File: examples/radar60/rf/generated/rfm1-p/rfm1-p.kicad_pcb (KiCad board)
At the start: 6 copper layers, 40.1 x 23.8 mm, 18 parts, among them U1 IWR6843AQGABLR (rings 0-2 of 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

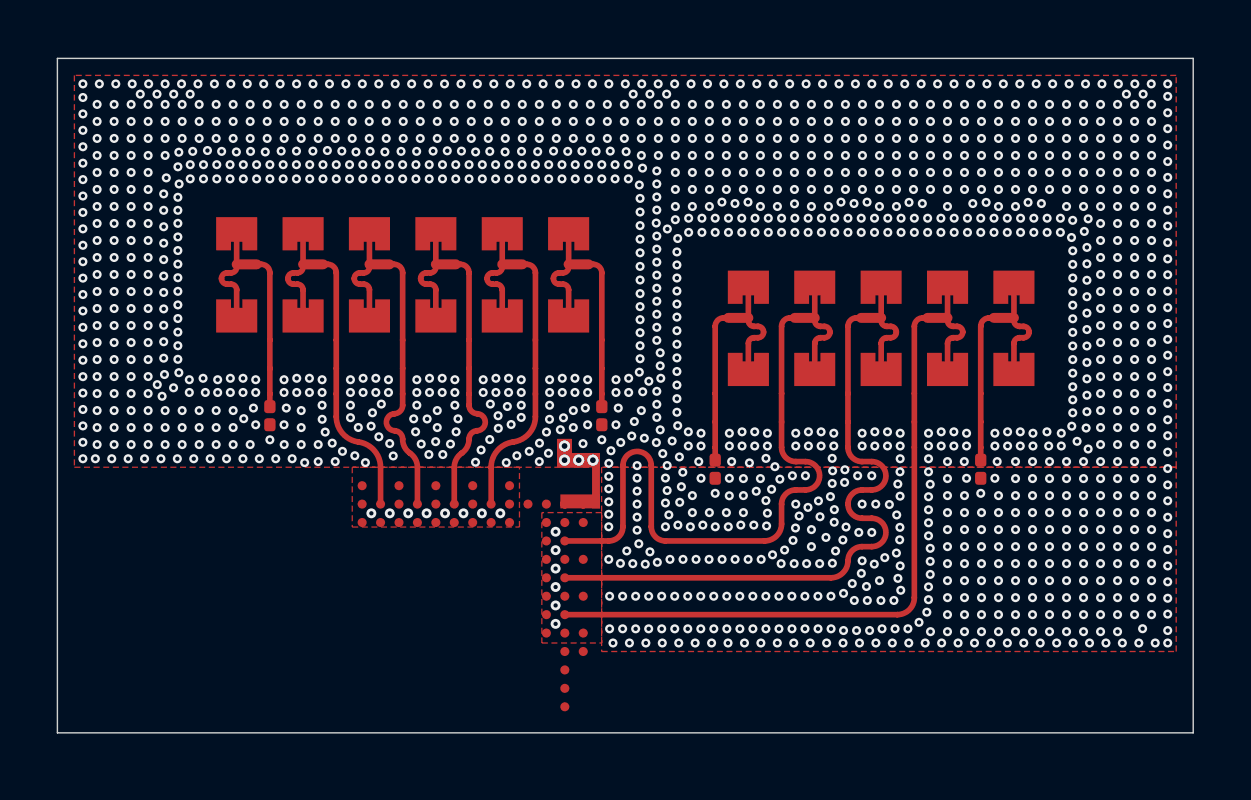
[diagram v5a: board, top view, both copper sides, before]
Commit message: radar60 rf: freeze macro v2 (stage 3b): C1 column pick, rfm1-m/n/p, coupons, board_frame
- rfmacro params: the C1 rule's pick (embedded centre column, cell-c1b-6, K0, 20 um):
  fullwave_l_scale 1.025, inset 0.325, w35 0.42, t_y 0.25. Worst in-band |S11| -6.5 dB
  (-7.2 dB Palace-referred); ANT-02 RL miss preregistered. K1 at L 1.00/1.015/1.03
  (s3b-e3) never reaches -10 dB (best -8.8 dB), so K0 stays per the K rule.
- regenerated rfm1-m/-n/-p and coupons with the frozen defaults (S1 outer dummies, D14 PA
  feed + fence, D15 A, C1); KiCad DRC 0 violations, 0 unconnected on all three.
- board/floorplan.yaml follows the new board_frame: height 47.40 (min 47.384), patches,
  region, pocket (now 1.69 x 1.55), guard, mounting holes; gen_board --macro all covered.
- tests: expectations updated for the S1 default (were failing at HEAD since the S1/fence
  freeze); series/T4 option tests pin S2 dummies (under S1 they leave a G4 fence gap).

Co-Authored-By: Claude Opus 5.5 <noreply@anthropic.com>
Claude-Session: https://claude.ai/code/session_01XmUgXgxLjzBpn2W6JpqE2p
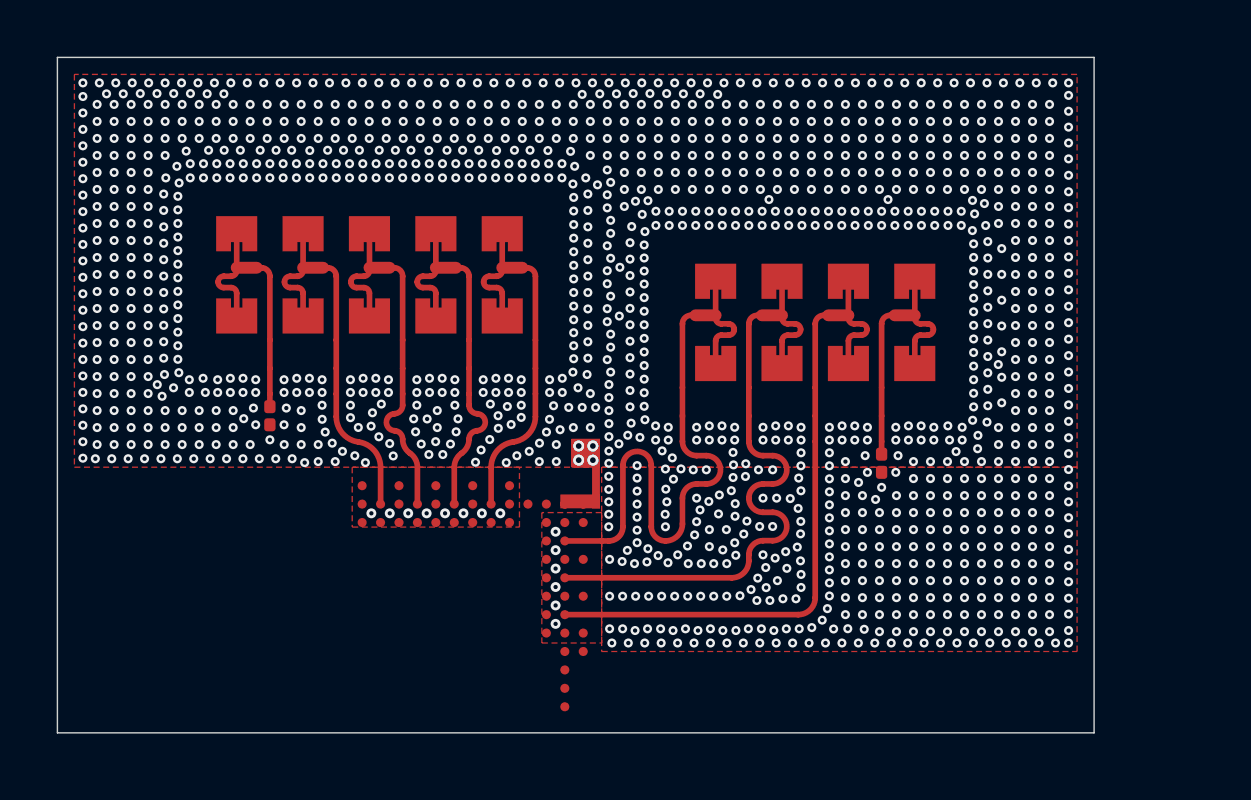
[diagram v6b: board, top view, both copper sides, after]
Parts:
- removed ANT_RXD5, ANT_TXD0: 2-patch corporate column, terminated dummy, radar60:COL2_DUMMY
- removed RT3, RT4: 50R 0201 thin film, radar60:R_0201_0603Metric_LOAD
- moved RT2 10.0 mm to (115.1, 94.7)
- moved ANT_TX1 3.50 mm to (109.2, 89.7)
- moved ANT_TX2 3.50 mm to (111.6, 89.7)
- moved ANT_TX3 3.50 mm to (113.9, 89.7)
- moved ANT_TXD4 3.50 mm to (116.2, 89.7)
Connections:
- RT2 pad 1: RXD5 -> TXD4
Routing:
- net TXD0: track 9.08 -> 0.00 mm
- net RXD5: track 9.08 -> 0.00 mm
- net TX2: track 26.2 -> 23.0 mm
- net TX1: track 26.2 -> 23.0 mm
- net TX3: track 26.6 -> 23.4 mm
- net GND: vias 1437 -> 1313
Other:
- board size 40.1 x 23.8 mm -> 36.6 x 23.8 mm
